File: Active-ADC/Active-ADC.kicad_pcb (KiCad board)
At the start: 4 copper layers, 17 x 13 mm, 18 parts, among them J1 FPGA Terminal, J2 ADC Terminal, Q1 BC847, Q2 BC847, Q3 BC847

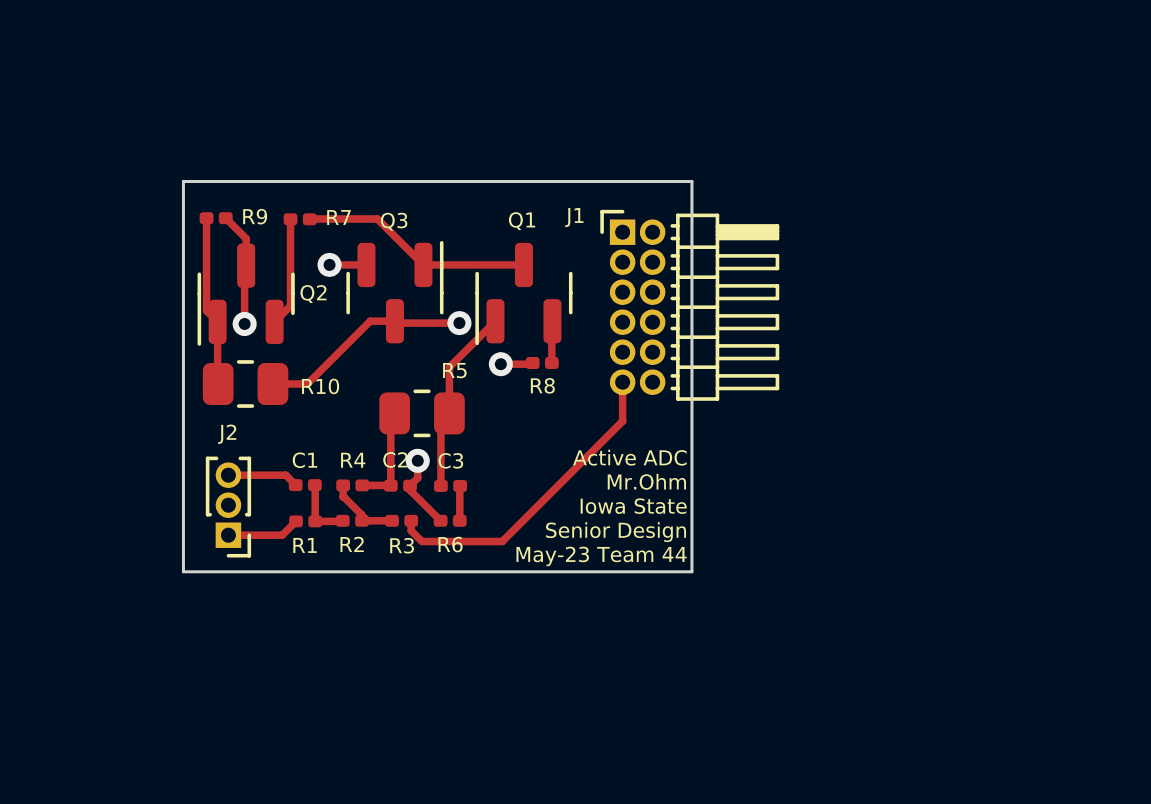
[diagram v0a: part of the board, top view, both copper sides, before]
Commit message: Updated footprints too all 0805 standard
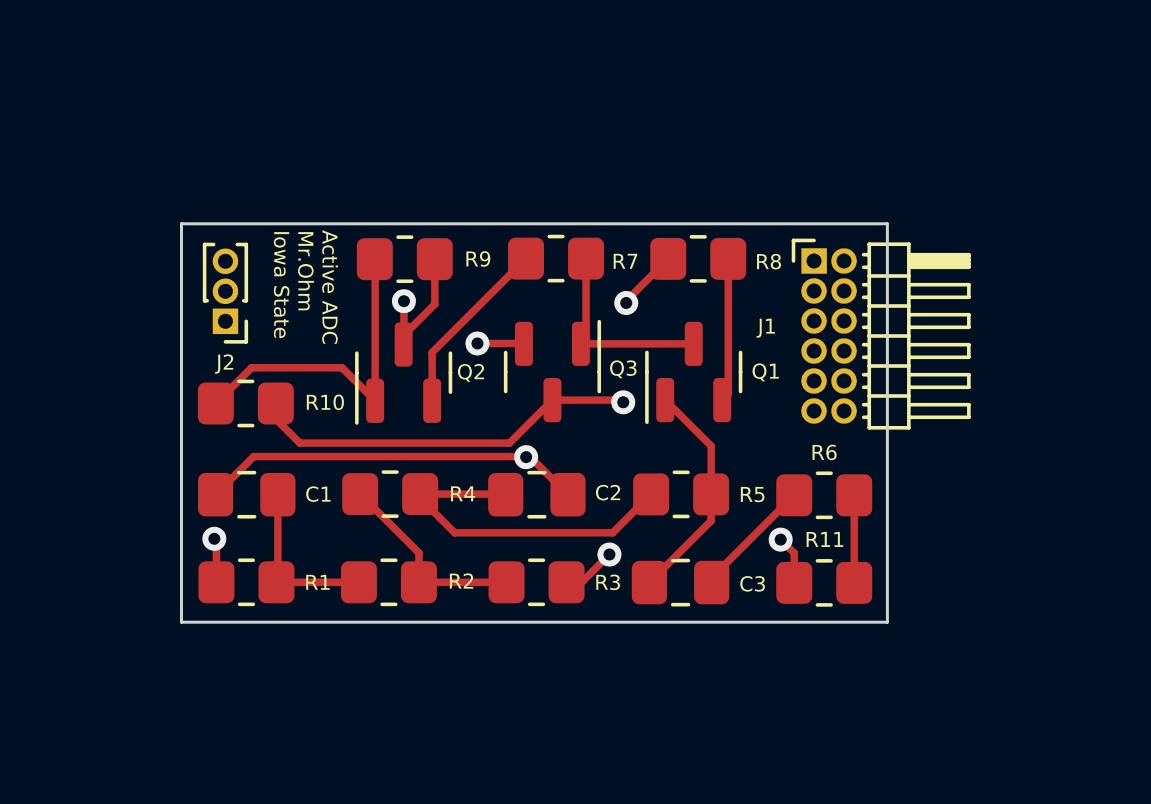
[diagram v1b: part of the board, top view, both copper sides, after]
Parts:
- added R11: 680, Resistor_SMD:R_0805_2012Metric_Pad1.20x1.40mm_HandSolder, F.Cu at (135.7, 92.3)
- C1, C2, C3: footprint Capacitor_SMD:C_0201_0603Metric -> Capacitor_SMD:C_0805_2012Metric_Pad1.18x1.45mm_HandSolder
- R1, R2, R3, R4, R7, R8, R9: footprint Resistor_SMD:R_0201_0603Metric -> Resistor_SMD:R_0805_2012Metric_Pad1.20x1.40mm_HandSolder
- R10, R5: footprint Resistor_SMD:R_0805_2012Metric -> Resistor_SMD:R_0805_2012Metric_Pad1.20x1.40mm_HandSolder
- R6: value 1170 -> 470; footprint Resistor_SMD:R_0201_0603Metric -> Resistor_SMD:R_0805_2012Metric_Pad1.20x1.40mm_HandSolder
- moved R6 12.5 mm to (135.7, 89.4), turned to 180 degrees
- moved R5 9.05 mm to (131.0, 89.3)
- moved R7 8.63 mm to (126.8, 81.5)
- moved C3 8.32 mm to (130.9, 92.3)
- moved J2 7.13 mm to (115.8, 83.6)
- moved J1 6.45 mm to (135.4, 81.5)
- moved R9 6.44 mm to (121.8, 81.5)
- moved R8 6.25 mm to (131.5, 81.5)
- moved Q1 6.24 mm to (131.4, 85.2)
- moved Q2 5.87 mm to (121.7, 85.3)
- moved Q3 5.87 mm to (126.7, 85.2)
- moved R3 4.94 mm to (126.2, 92.3)
- moved C2 4.56 mm to (126.2, 89.3)
- moved R1 2.83 mm to (116.5, 92.3)
- moved R2 2.38 mm to (121.2, 92.3)
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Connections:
- R6 pad 1: GND -> Net-(R6-Pad1)
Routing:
- net GND: track 7.22 -> 18.0 mm, vias 3 -> 4
- net Net-(C2-Pad1): track 3.42 -> 11.7 mm
- net /Sensor-IN: track 2.44 -> 8.88 mm, vias 0 -> 1
- net Net-(Q2-Pad1): track 5.69 -> 11.0 mm
- net /FPGA-OUT: track 14.5 -> 19.7 mm
- net Net-(R2-Pad2): track 2.46 -> 6.67 mm
- net Net-(C1-Pad1): track 2.11 -> 5.69 mm
- net Net-(Q1-Pad2): track 1.40 -> 4.79 mm
- net Net-(R6-Pad1): track 0.00 -> 2.92 mm
- net Net-(C3-Pad2): track 1.16 -> 4.05 mm
- net Net-(Q2-Pad2): track 3.64 -> 6.04 mm
- net /SIGMA-CHERRY: track 6.25 -> 7.57 mm
- net Net-(Q1-Pad3): track 7.78 -> 6.70 mm
- net /3.3V: track 3.83 -> 4.72 mm
- net /FPGA-IN: track 10.5 -> 10.6 mm, vias 0 -> 1
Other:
- board size 17 x 13 mm -> 23.5 x 13.3 mm
- board text added: "Active ADC Mr.Ohm Iowa State"
- board text removed: "Active ADC Mr.Ohm Iowa State Senior Design May-23 Team 44"

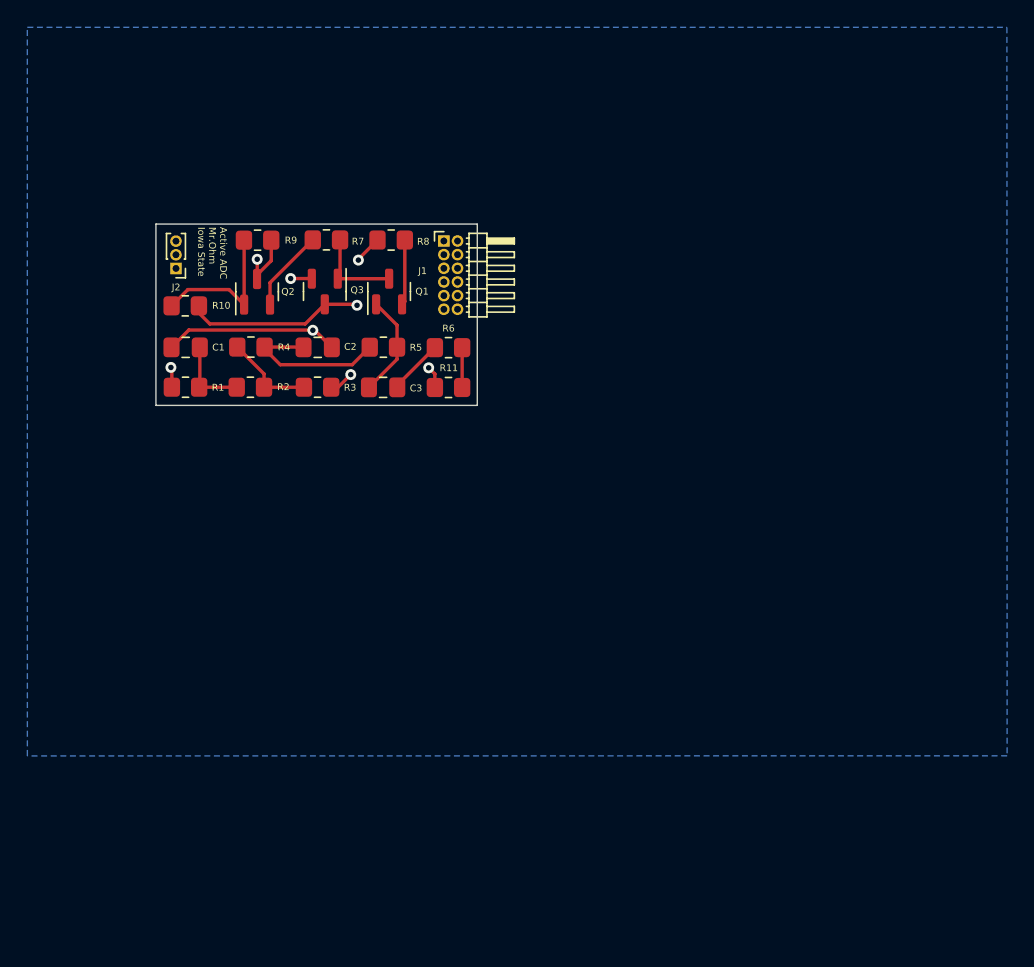
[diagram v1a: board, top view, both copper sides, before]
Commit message: Close to final pcb adjusted footprints and layout design incorperating voltage divider
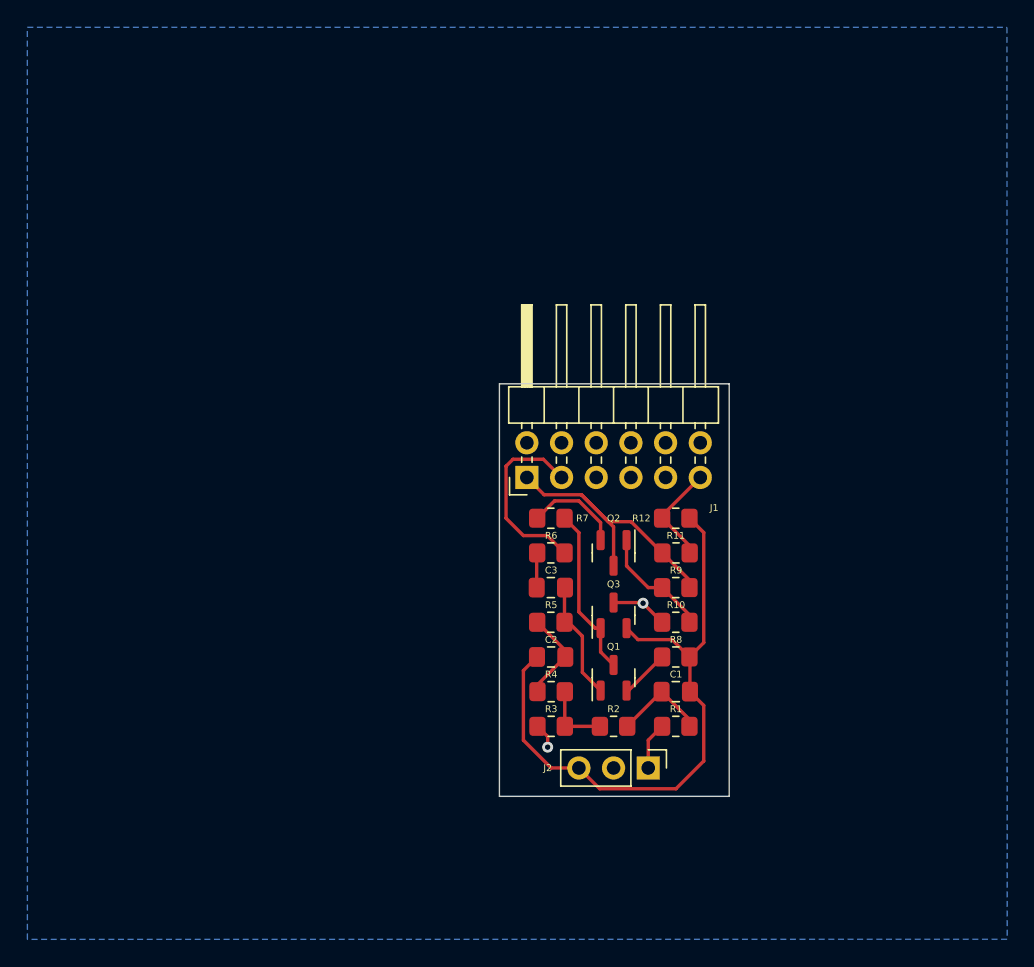
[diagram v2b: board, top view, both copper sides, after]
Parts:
- added R12: 3.3k, Resistor_SMD:R_0805_2012Metric_Pad1.20x1.40mm_HandSolder, F.Cu at (152.4, 101.9)
- J1: footprint Connector_PinHeader_1.00mm:PinHeader_2x06_P1.00mm_Horizontal -> Connector_PinHeader_2.54mm:PinHeader_2x06_P2.54mm_Horizontal
- J2: footprint Connector_PinHeader_1.00mm:PinHeader_1x03_P1.00mm_Vertical -> Connector_PinHeader_2.54mm:PinHeader_1x03_P2.54mm_Vertical
- R11: value 680 -> 6.8k
- R6: value 470 -> 1.1k
- moved J2 50.3 mm to (150.4, 120.1), turned to -90 degrees
- moved C1 43.9 mm to (152.4, 114.6), turned to 0 degrees
- moved R1 43.7 mm to (152.4, 117.1)
- moved R10 42.8 mm to (152.4, 109.5), turned to 180 degrees
- moved R9 39.8 mm to (152.4, 106.9)
- moved R8 37.0 mm to (152.4, 112.0), turned to 0 degrees
- moved R2 36.4 mm to (147.8, 117.1), turned to 180 degrees
- moved R4 33.5 mm to (143.3, 114.6), turned to 180 degrees
- moved Q1 32.7 mm to (147.8, 113.5)
- moved Q2 32.4 mm to (147.8, 104.4), turned to -90 degrees
- moved Q3 31.8 mm to (147.8, 109.0), turned to 90 degrees
- moved R3 30.2 mm to (143.3, 117.1), turned to 0 degrees
- moved C2 28.4 mm to (143.3, 112.0), turned to 180 degrees
- moved R7 26.2 mm to (143.2, 101.9)
- moved R5 23.6 mm to (143.2, 109.5)
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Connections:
- J1 pad 11: /FPGA-IN -> /FPGA-REF
- J1 pad 7: unconnected-(J1-Pad7) -> /FPGA-OUT
- J1 pad 9: /FPGA-OUT -> /FPGA-IN
- R11 pad 1: GND -> /3.3V
- R11 pad 2: Net-(R6-Pad1) -> /FPGA-REF
- R6 pad 1: Net-(R6-Pad1) -> GND
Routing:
- net GND: track 18.0 -> 60.6 mm, vias 4 -> 0
- net /FPGA-IN: track 10.6 -> 29.0 mm
- net /3.3V: track 4.72 -> 21.7 mm, vias 1 -> 0
- net /FPGA-REF: track 0.00 -> 7.52 mm
- net /FPGA-OUT: track 19.7 -> 13.7 mm
- net Net-(Q1-Pad3): track 6.70 -> 12.5 mm
- net /Sensor-IN: track 8.88 -> 3.47 mm, vias 1 -> 0
- net Net-(C2-Pad1): track 11.7 -> 6.78 mm
- net Net-(R6-Pad1): track 2.92 -> 0.00 mm
- net Net-(Q2-Pad1): track 11.0 -> 8.52 mm
- net Net-(R2-Pad2): track 6.67 -> 5.11 mm
- net Net-(C3-Pad2): track 4.05 -> 2.56 mm
- net Net-(C1-Pad1): track 5.69 -> 6.97 mm
- net Net-(Q2-Pad2): track 6.04 -> 7.11 mm
- net Net-(Q1-Pad2): track 4.79 -> 3.74 mm
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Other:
- board size 23.5 x 13.3 mm -> 16.8 x 30.2 mm
- board text removed: "Active ADC Mr.Ohm Iowa State"

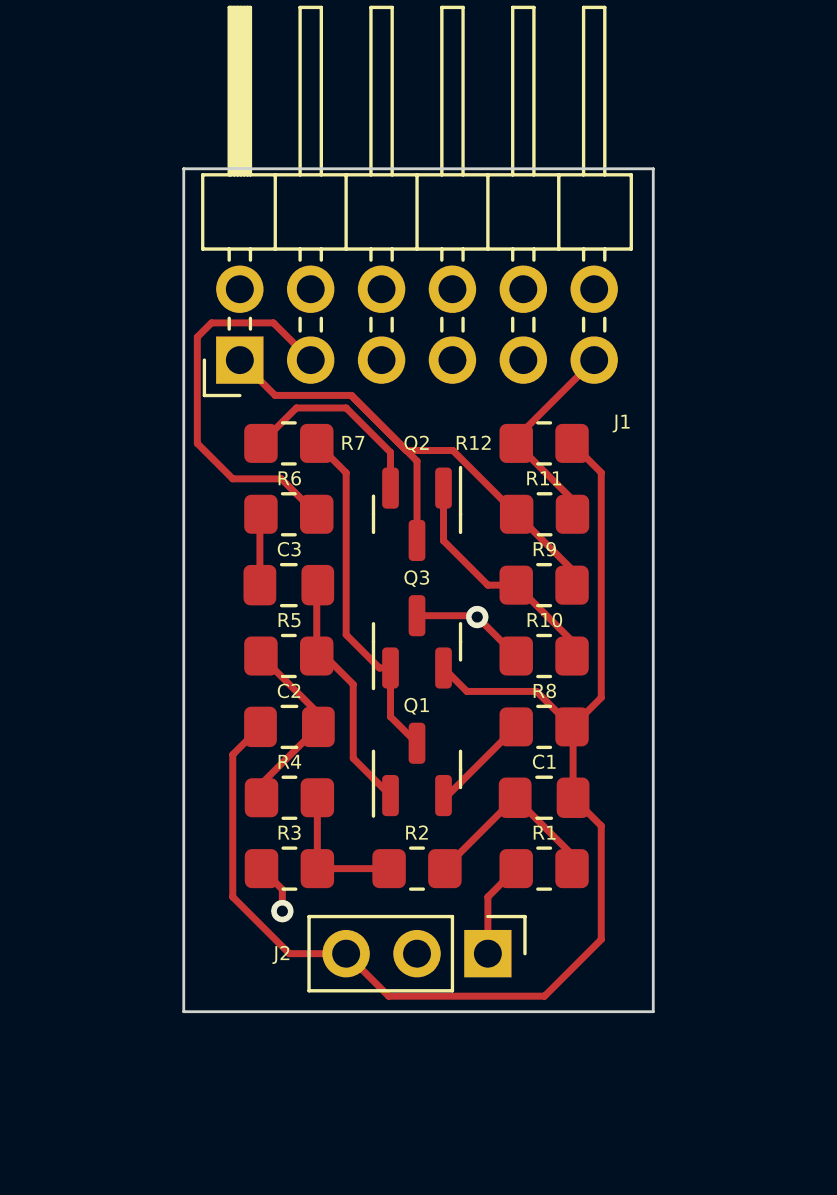
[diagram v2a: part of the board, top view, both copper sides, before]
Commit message: Updated models with new schematic details
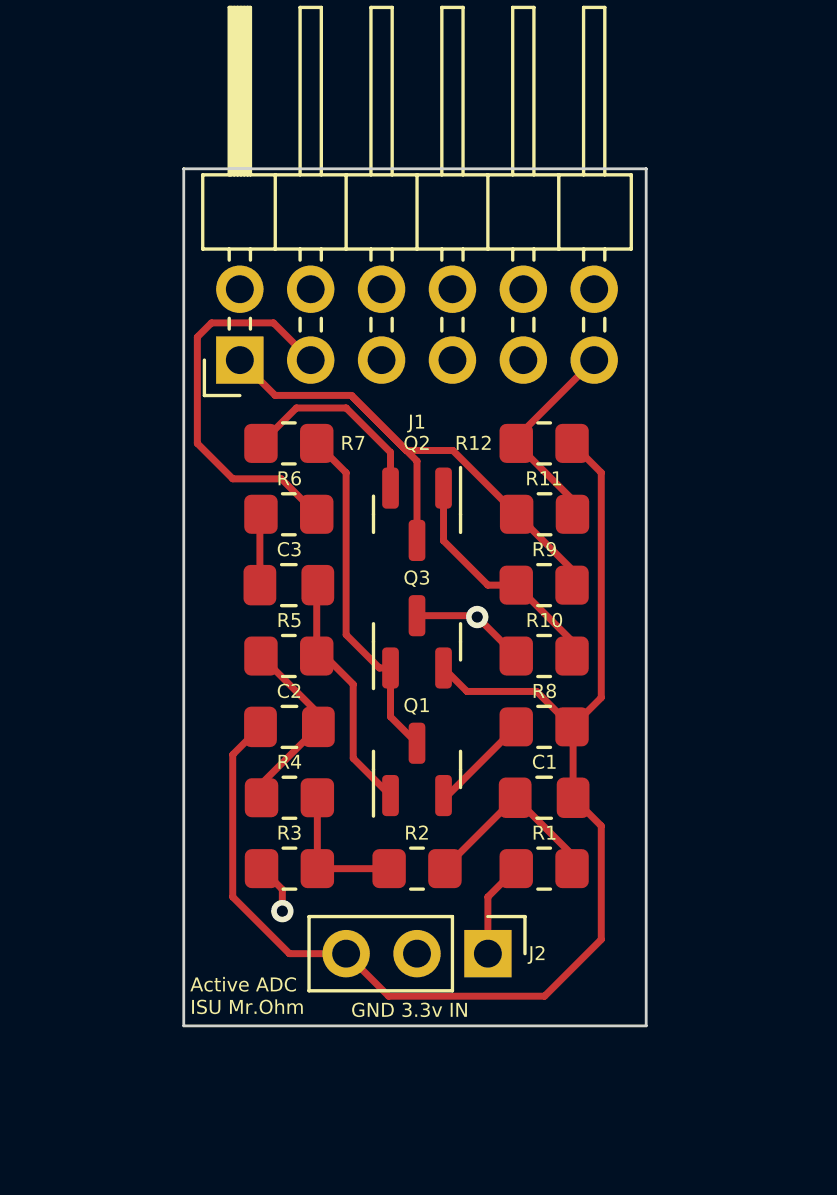
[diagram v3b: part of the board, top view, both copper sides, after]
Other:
- board size 16.8 x 30.2 mm -> 16.6 x 30.7 mm
- board text added: "Active ADC ISU Mr.Ohm"
- board text added: "GND 3.3v IN"
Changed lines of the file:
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@@
       (effects (font (size 0.5 0.5) (thickness 0.125)))
     )
-    (fp_text value "BC847" (at 2.54 21.336 90) (layer "F.Fab")
+    (fp_text value "BC847" (at 17.018 82.026 90) (layer "F.Fab")
       (effects (font (size 1 1) (thickness 0.15)))
     )
@@
       (effects (font (size 0.5 0.5) (thickness 0.125)))
     )
-    (fp_text value "2.1k" (at -44.958 -9.144) (layer "F.Fab")
+    (fp_text value "2.1k" (at -105.648 5.334) (layer "F.Fab")
       (effects (font (size 1 1) (thickness 0.15)))
     )
@@
       (effects (font (size 0.5 0.5) (thickness 0.125)))
     )
-    (fp_text value "6.8k" (at 30.988 16.256) (layer "F.Fab")
+    (fp_text value "6.8k" (at 63.5 16.002) (layer "F.Fab")
       (effects (font (size 1 1) (thickness 0.15)))
     )
@@
       (effects (font (size 0.5 0.5) (thickness 0.125)))
     )
-    (fp_text value "15k" (at 24.426 10.474) (layer "F.Fab")
+    (fp_text value "15k" (at 85.116 -4.004) (layer "F.Fab")
       (effects (font (size 1 1) (thickness 0.15)))
     )
@@
       (effects (font (size 0.5 0.5) (thickness 0.125)))
     )
-    (fp_text value "470p" (at -28.956 2.286) (layer "F.Fab")
+    (fp_text value "470p" (at -61.468 2.54) (layer "F.Fab")
       (effects (font (size 1 1) (thickness 0.15)))
     )
@@
       (effects (font (size 0.5 0.5) (thickness 0.125)))
     )
-    (fp_text value "2.5k" (at 23.114 -3.302) (layer "F.Fab")
+    (fp_text value "2.5k" (at 83.804 -17.78) (layer "F.Fab")
       (effects (font (size 1 1) (thickness 0.15)))
     )
@@
       (effects (font (size 0.5 0.5) (thickness 0.125)))
     )
-    (fp_text value "100" (at 27.686 17.78) (layer "F.Fab")
+    (fp_text value "100" (at 60.198 17.526) (layer "F.Fab")
       (effects (font (size 1 1) (thickness 0.15)))
     )
@@
       (effects (font (size 0.5 0.5) (thickness 0.125)))
     )
-    (fp_text value "330" (at -26.416 22.606) (layer "F.Fab")
+    (fp_text value "330" (at -87.106 37.084) (layer "F.Fab")
       (effects (font (size 1 1) (thickness 0.15)))
     )
@@
       (effects (font (size 0.5 0.5) (thickness 0.125)))
     )
-    (fp_text value "68p" (at -60.198 -27.94) (layer "F.Fab")
+    (fp_text value "68p" (at -92.71 -27.686) (layer "F.Fab")
       (effects (font (size 1 1) (thickness 0.15)))
     )
@@
       (effects (font (size 0.5 0.5) (thickness 0.125)))
     )
-    (fp_text value "1.5k" (at -62.992 -10.16) (layer "F.Fab")
+    (fp_text value "1.5k" (at -95.504 -9.906) (layer "F.Fab")
       (effects (font (size 1 1) (thickness 0.15)))
     )
@@
       (effects (font (size 0.5 0.5) (thickness 0.125)))
     )
-    (fp_text value ".1u" (at 47.752 -4.572) (layer "F.Fab")
+    (fp_text value ".1u" (at 80.264 -4.826) (layer "F.Fab")
       (effects (font (size 1 1) (thickness 0.15)))
     )
@@
       (effects (font (size 0.5 0.5) (thickness 0.125)))
     )
-    (fp_text value "15k" (at -38.608 2.032) (layer "F.Fab")
+    (fp_text value "15k" (at -99.298 16.51) (layer "F.Fab")
       (effects (font (size 1 1) (thickness 0.15)))
     )
@@
     (property "Sheetname" "")
     (attr through_hole)
-    (fp_text reference "J1" (at -2.224 13.716 180) (layer "F.SilkS")
-      (effects (font (size 0.5 0.5) (thickness 0.125)))
-    )
-    (fp_text value "FPGA Terminal" (at 28.194 18.288 90) (layer "F.Fab")
+    (fp_text reference "J1" (at -2.224 6.35 180) (layer "F.SilkS")
+      (effects (font (size 0.5 0.5) (thickness 0.125)))
+    )
+    (fp_text value "FPGA Terminal" (at -12.892 -74.676 90) (layer "F.Fab")
       (effects (font (size 1 1) (thickness 0.15)))
     )
@@
       (effects (font (size 0.5 0.5) (thickness 0.125)))
     )
-    (fp_text value "18k" (at -24.892 34.036) (layer "F.Fab")
+    (fp_text value "18k" (at -57.404 34.29) (layer "F.Fab")
       (effects (font (size 1 1) (thickness 0.15)))
     )
@@
       (effects (font (size 0.5 0.5) (thickness 0.125)))
     )
-    (fp_text value "3.3k" (at -37.83 6.858) (layer "F.Fab")
+    (fp_text value "3.3k" (at -98.52 21.336) (layer "F.Fab")
       (effects (font (size 1 1) (thickness 0.15)))
     )
@@
       (effects (font (size 0.5 0.5) (thickness 0.125)))
     )
-    (fp_text value "8k" (at -7.62 20.828) (layer "F.Fab")
+    (fp_text value "8k" (at -68.31 35.306) (layer "F.Fab")
       (effects (font (size 1 1) (thickness 0.15)))
     )
@@
       (effects (font (size 0.5 0.5) (thickness 0.125)))
     )
-    (fp_text value "BC847" (at 36.322 -4.572 90) (layer "F.Fab")
+    (fp_text value "BC847" (at -4.764 -97.536 90) (layer "F.Fab")
       (effects (font (size 1 1) (thickness 0.15)))
     )
@@
       (effects (font (size 0.5 0.5) (thickness 0.125)))
     )
-    (fp_text value "1.1k" (at -54.3775 0) (layer "F.Fab")
+    (fp_text value "1.1k" (at -86.8895 0.254) (layer "F.Fab")
       (effects (font (size 1 1) (thickness 0.15)))
     )
@@
       (effects (font (size 0.5 0.5) (thickness 0.125)))
     )
-    (fp_text value "BC847" (at 7.366 -34.29 90) (layer "F.Fab")
+    (fp_text value "BC847" (at -7.112 -94.98 90) (layer "F.Fab")
       (effects (font (size 1 1) (thickness 0.15)))
     )
@@
     (property "Sheetname" "")
     (attr through_hole)
-    (fp_text reference "J2" (at 0 7.366 180) (layer "F.SilkS")
+    (fp_text reference "J2" (at 0 -1.778 180) (layer "F.SilkS")
       (effects (font (size 0.5 0.5) (thickness 0.125)))
     )
@@
     )
   )
-  (gr_rect (start 139.468 92.012) (end 156.296 122.222) (layer "Edge.Cuts") (width 0.1) (fill none))
+  (gr_rect (start 139.468 92.012) (end 156.042 122.73) (layer "Edge.Cuts") (width 0.1) (fill none))
+  (gr_text "GND 3.3v IN" (at 147.574 122.174) (layer "F.SilkS")
+    (effects (font (size 0.5 0.5) (thickness 0.125)))
+  )
+  (gr_text "Active ADC\nISU Mr.Ohm \n" (at 139.7 121.666) (layer "F.SilkS")
+    (effects (font (size 0.5 0.5) (thickness 0.125)) (justify left))
+  )
   (segment (start 148.828 117.0725) (end 151.3465 114.554) (width 0.25) (layer "F.Cu") (net 1))
   (segment (start 153.384 117.094) (end 153.384 116.5915) (width 0.25) (layer "F.Cu") (net 1))
